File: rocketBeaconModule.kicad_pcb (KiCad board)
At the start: 2 copper layers, 57.1 x 57.2 mm, 97 parts, among them J1 TYPE-C-31-M-12, J2 PWR, J3 GND, J4 PWR, J5 GND, U1 STM32F401CCU6, U2 CP2102N-Axx-xQFN20, U3 CC1200, U4 MCP6001-OT, U8 MCP41010, X1 40MHz, Y1 16MHz

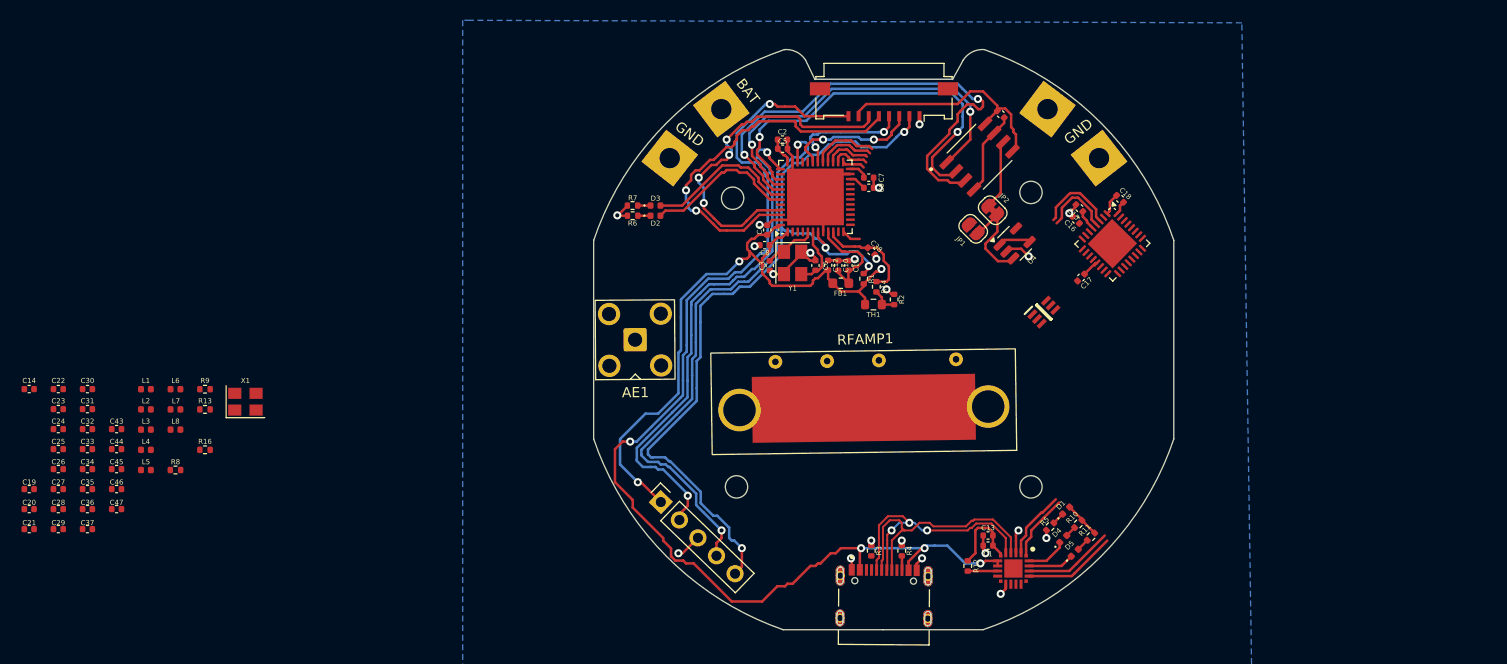
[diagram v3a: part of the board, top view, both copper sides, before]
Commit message: finished majority of routing other than matching network and amplifier/switch/antenna
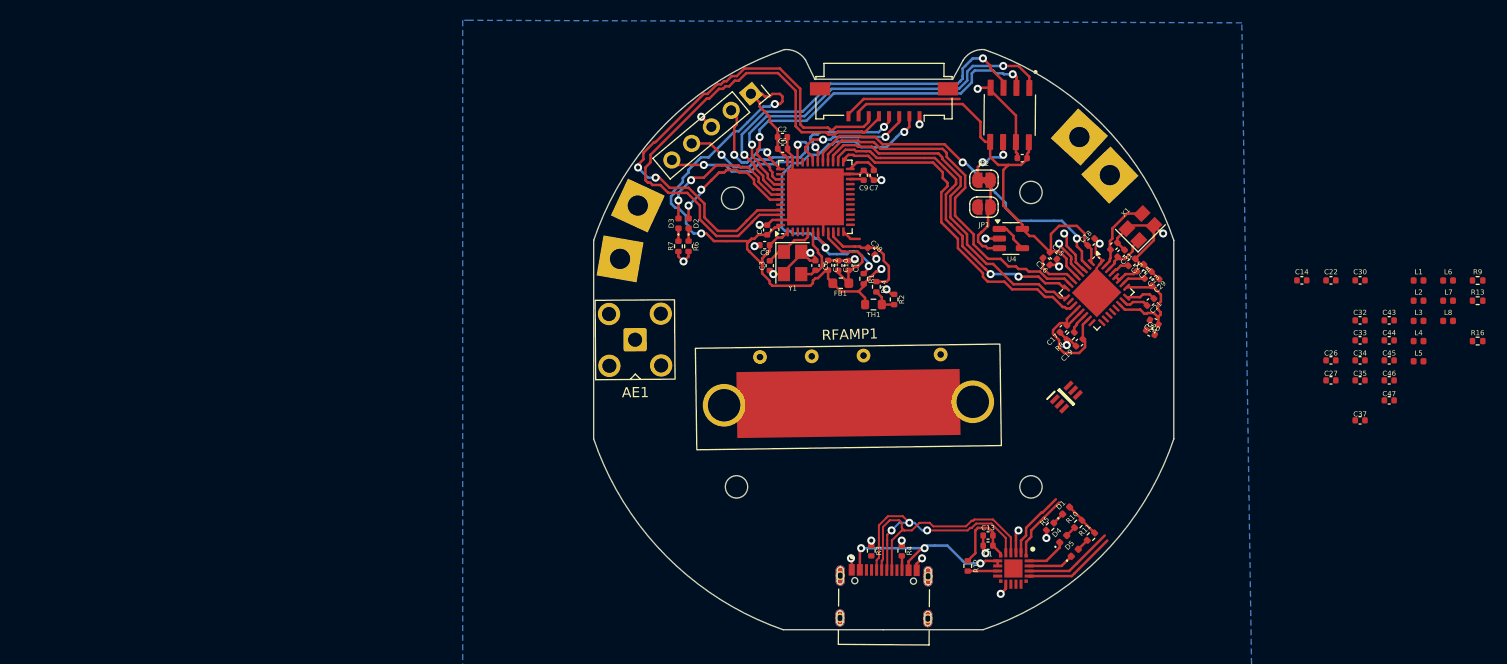
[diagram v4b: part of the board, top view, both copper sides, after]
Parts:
- moved C30 125.8 mm to (204.2, 90.6)
- moved C32 125.8 mm to (204.2, 94.6)
- moved C33 125.8 mm to (204.2, 96.5)
- moved C34 125.8 mm to (204.2, 98.5)
- moved C35 125.8 mm to (204.2, 100.5)
- moved C37 125.8 mm to (204.2, 104.4)
- moved C43 125.8 mm to (207.0, 94.6)
- moved C44 125.8 mm to (207.0, 96.5)
- moved C45 125.8 mm to (207.0, 98.5)
- moved C46 125.8 mm to (207.0, 100.5)
- moved C47 125.8 mm to (207.0, 102.4)
- moved C14 125.8 mm to (198.4, 90.6)
- moved C22 125.8 mm to (201.3, 90.6)
- moved C26 125.8 mm to (201.3, 98.5)
- moved C27 125.8 mm to (201.3, 100.5)
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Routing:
- net VBUS: track 110.7 -> 31.8 mm, vias 5 -> 3
- net +3.3V: track 109.1 -> 158.0 mm
- net /SWDIO: track 56.8 -> 16.6 mm
- net /SWCLK: track 51.0 -> 12.2 mm
- net /NRST: track 81.8 -> 47.9 mm
- net RADIO_CS: track 2.24 -> 33.8 mm
- net SPI2_MISO: track 4.49 -> 34.7 mm
- net SPI_MOSI: track 5.62 -> 35.6 mm
- net SPI2_SCK: track 3.71 -> 33.2 mm, vias 0 -> 2
- net RADIO_RESET: track 6.60 -> 34.4 mm, vias 0 -> 2
- net GND: track 66.3 -> 88.8 mm, vias 21 -> 25
- net /S1: track 34.4 -> 51.1 mm, vias 4 -> 2
- net /S2: track 36.6 -> 51.3 mm, vias 2 -> 0
- net SPIDATA: track 48.7 -> 38.6 mm
- net Net-(U3-XOSC_Q2): track 0.00 -> 7.59 mm
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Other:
- board text removed: "BAT"
- board text removed: "GND"

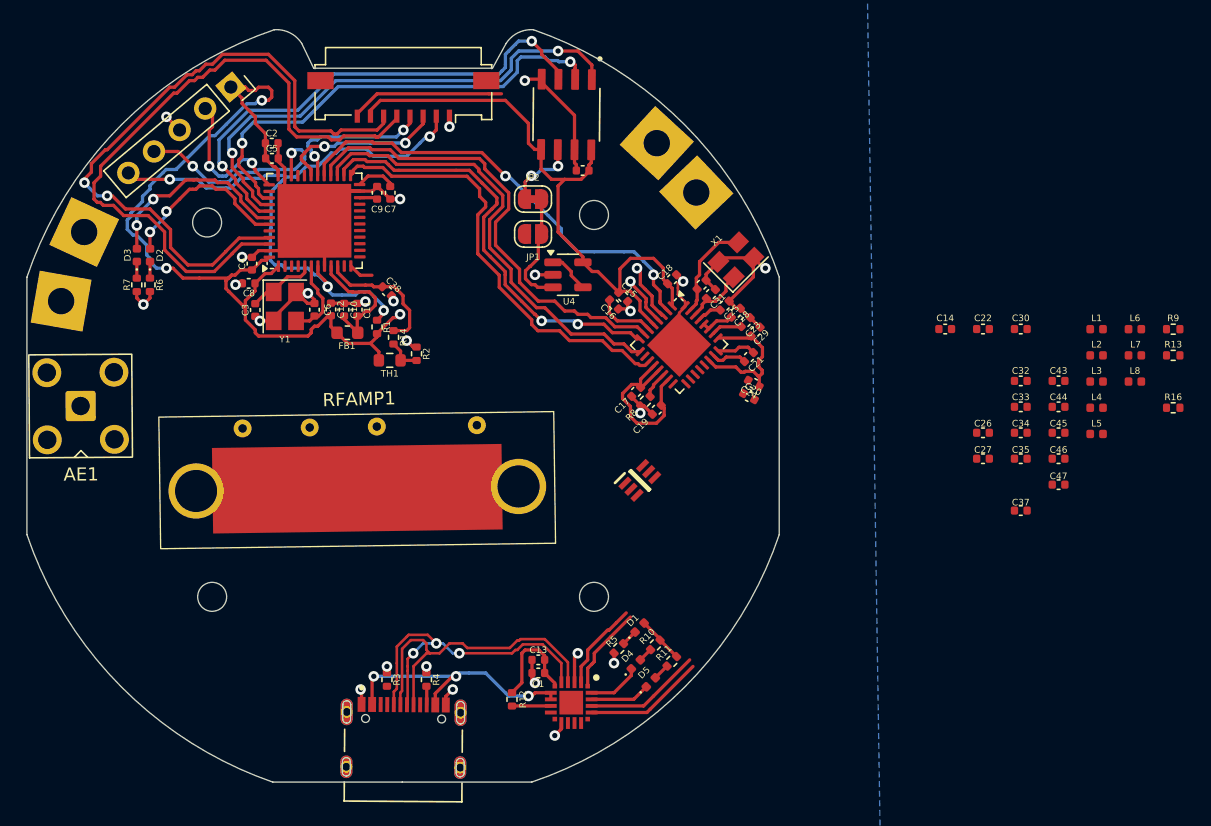
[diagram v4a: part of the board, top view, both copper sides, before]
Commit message: finished routing pcb and passed DRC, waiting for review by Ethan
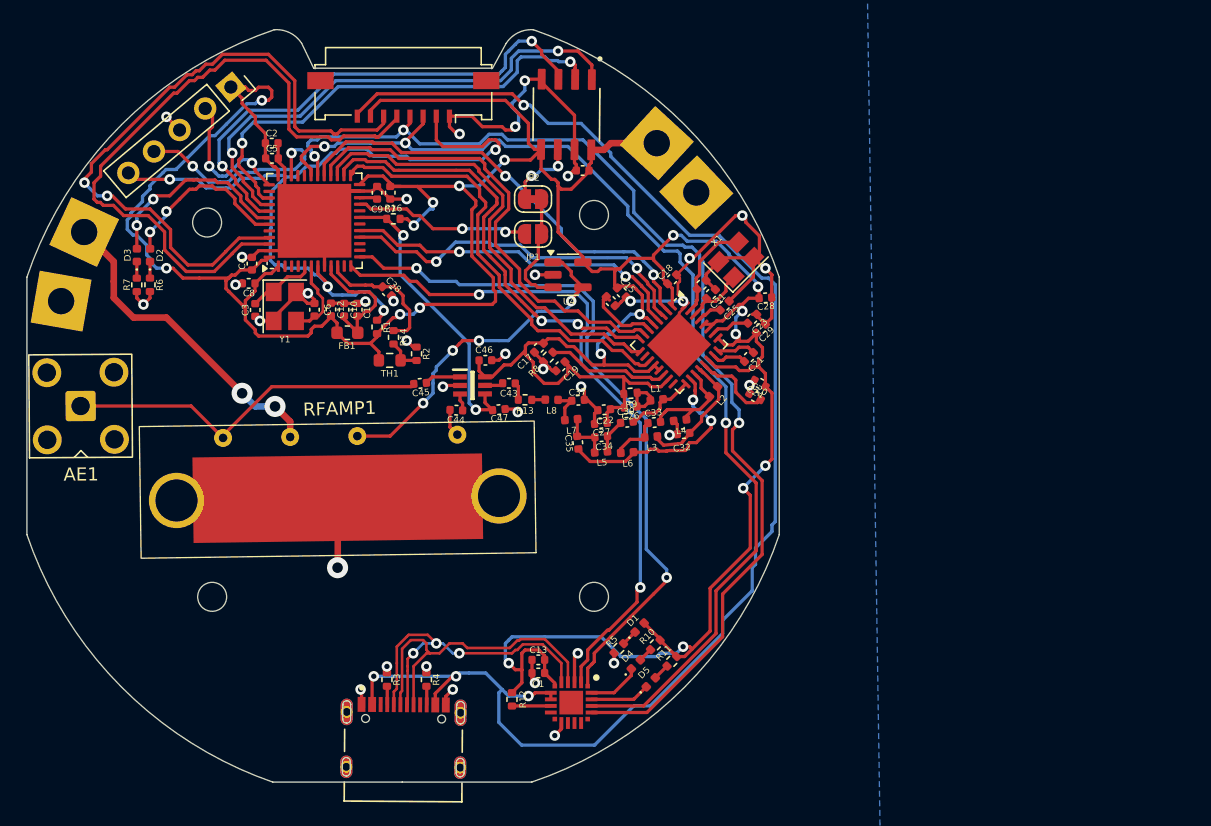
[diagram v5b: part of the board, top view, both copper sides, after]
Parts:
- removed C14: DNM, Capacitor_SMD:C_0402_1005Metric
- moved R16 61.0 mm to (156.5, 82.2)
- moved R13 49.4 mm to (166.5, 96.0), turned to 179.2 degrees
- moved C45 48.6 mm to (158.5, 94.8), turned to -175.2 degrees
- moved C44 45.8 mm to (161.3, 96.8), turned to 177.6 degrees
- moved L8 44.3 mm to (168.5, 96.0), turned to 179.2 degrees
- moved C46 44.2 mm to (163.5, 93.0), turned to -179.2 degrees
- moved L7 43.1 mm to (170.0, 97.5), turned to -175.2 degrees
- moved C47 42.9 mm to (164.5, 96.7), turned to -175.2 degrees
- moved C43 41.8 mm to (165.3, 94.7), turned to 179.2 degrees
- moved R9 41.5 mm to (174.5, 95.5), turned to -175.2 degrees
- moved L6 39.7 mm to (174.2, 100.0), turned to -176.8 degrees
- moved L5 37.7 mm to (172.3, 100.0), turned to -175.2 degrees
- moved C37 34.7 mm to (170.5, 96.0), turned to 4 degrees
- moved L3 34.1 mm to (176.1, 98.8), turned to -175.2 degrees
- moved L1 33.8 mm to (176.5, 96.0), turned to 5.6 degrees
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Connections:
- RFAMP1 pad MH1: (no net) -> GND
- RFAMP1 pad MH2: (no net) -> GND
- U1 pad 21: unconnected-(U1-PB10-Pad21) -> AMP_ON
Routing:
- net +3.3V: track 158.0 -> 290.7 mm, vias 3 -> 18
- net VBUS: track 31.8 -> 110.8 mm, vias 3 -> 4
- net /TX: track 21.1 -> 85.0 mm, vias 2 -> 3
- net /RX: track 21.6 -> 82.3 mm, vias 2 -> 3
- net /CP2102N_SIG2: track 6.60 -> 53.6 mm, vias 0 -> 2
- net GND: track 88.8 -> 134.3 mm, vias 25 -> 36
- net /CP2102N_SIG1: track 8.85 -> 52.3 mm, vias 0 -> 2
- net Net-(AE1-A): track 0.00 -> 28.1 mm
- net +BATT: track 0.00 -> 24.6 mm, vias 0 -> 2
- net RADIO_MARC_INT: track 4.44 -> 27.7 mm, vias 1 -> 2
- net Net-(RFAMP1-GATE_VOLTAGE_(VGG)): track 3.24 -> 26.3 mm, vias 0 -> 4
- net RADIO_INT: track 3.83 -> 26.3 mm, vias 1 -> 2
- net VCTL: track 0.00 -> 22.4 mm, vias 0 -> 2
- net Net-(U3-TRX_SW): track 0.00 -> 16.8 mm, vias 0 -> 2
- net AMP_ON: track 0.00 -> 13.5 mm, vias 0 -> 2
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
